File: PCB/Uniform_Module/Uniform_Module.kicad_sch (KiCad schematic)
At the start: 159 parts, among them U1 STM32L072KZT6, U2 SN74AHCT1G125DBVR

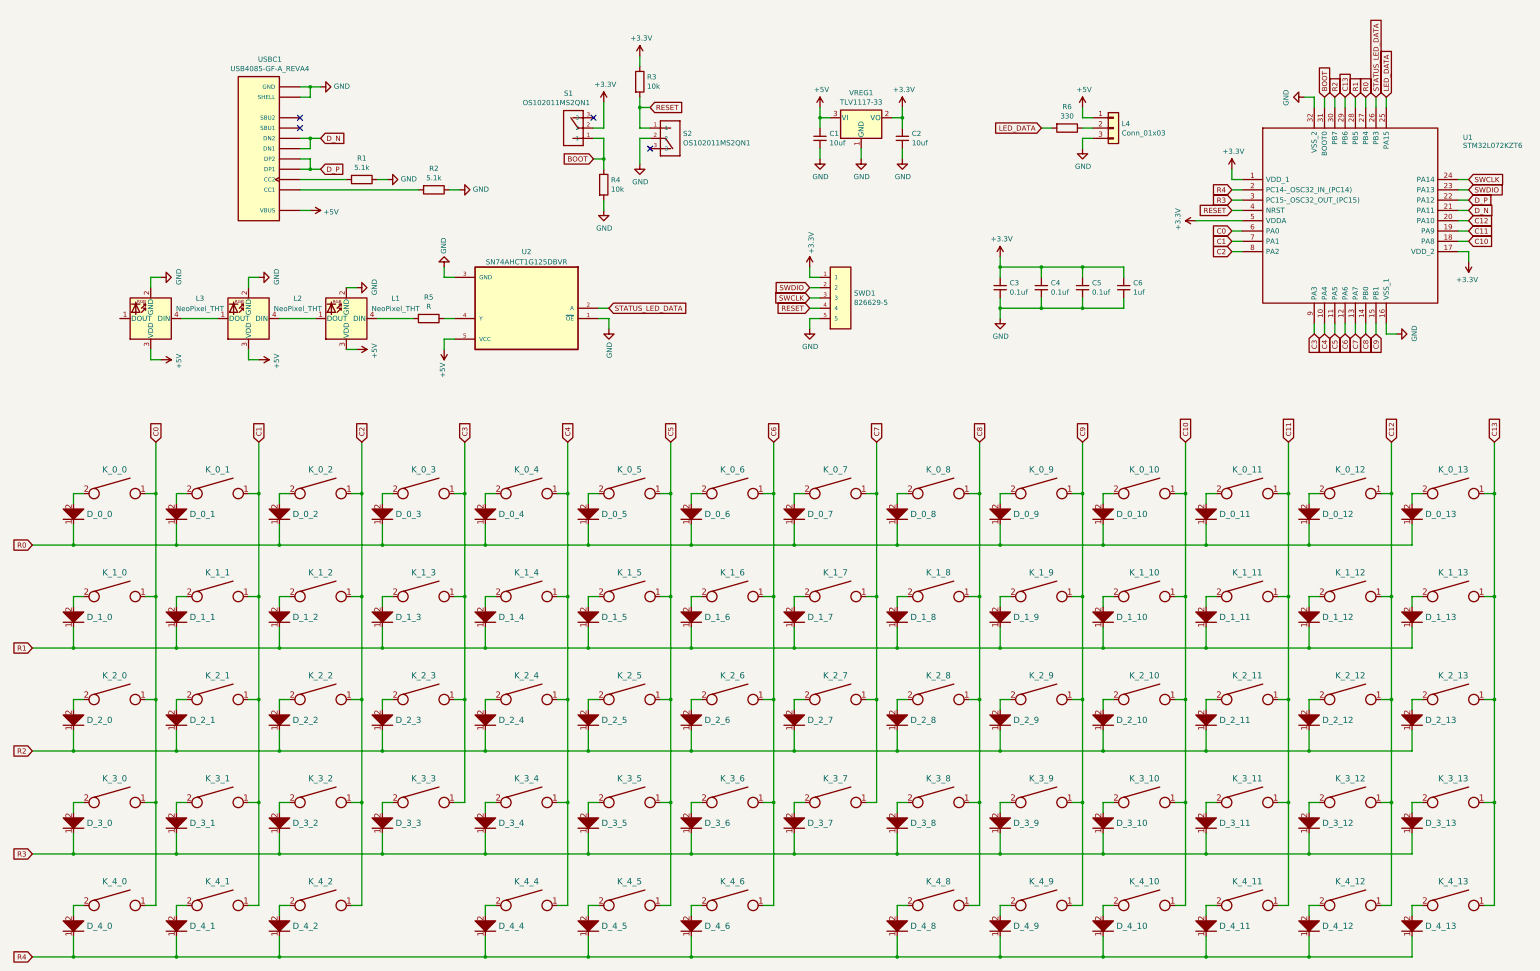
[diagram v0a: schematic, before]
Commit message: broke Uniform into two projects - uniform_board and uniform_module. Finished uniform_module schematic
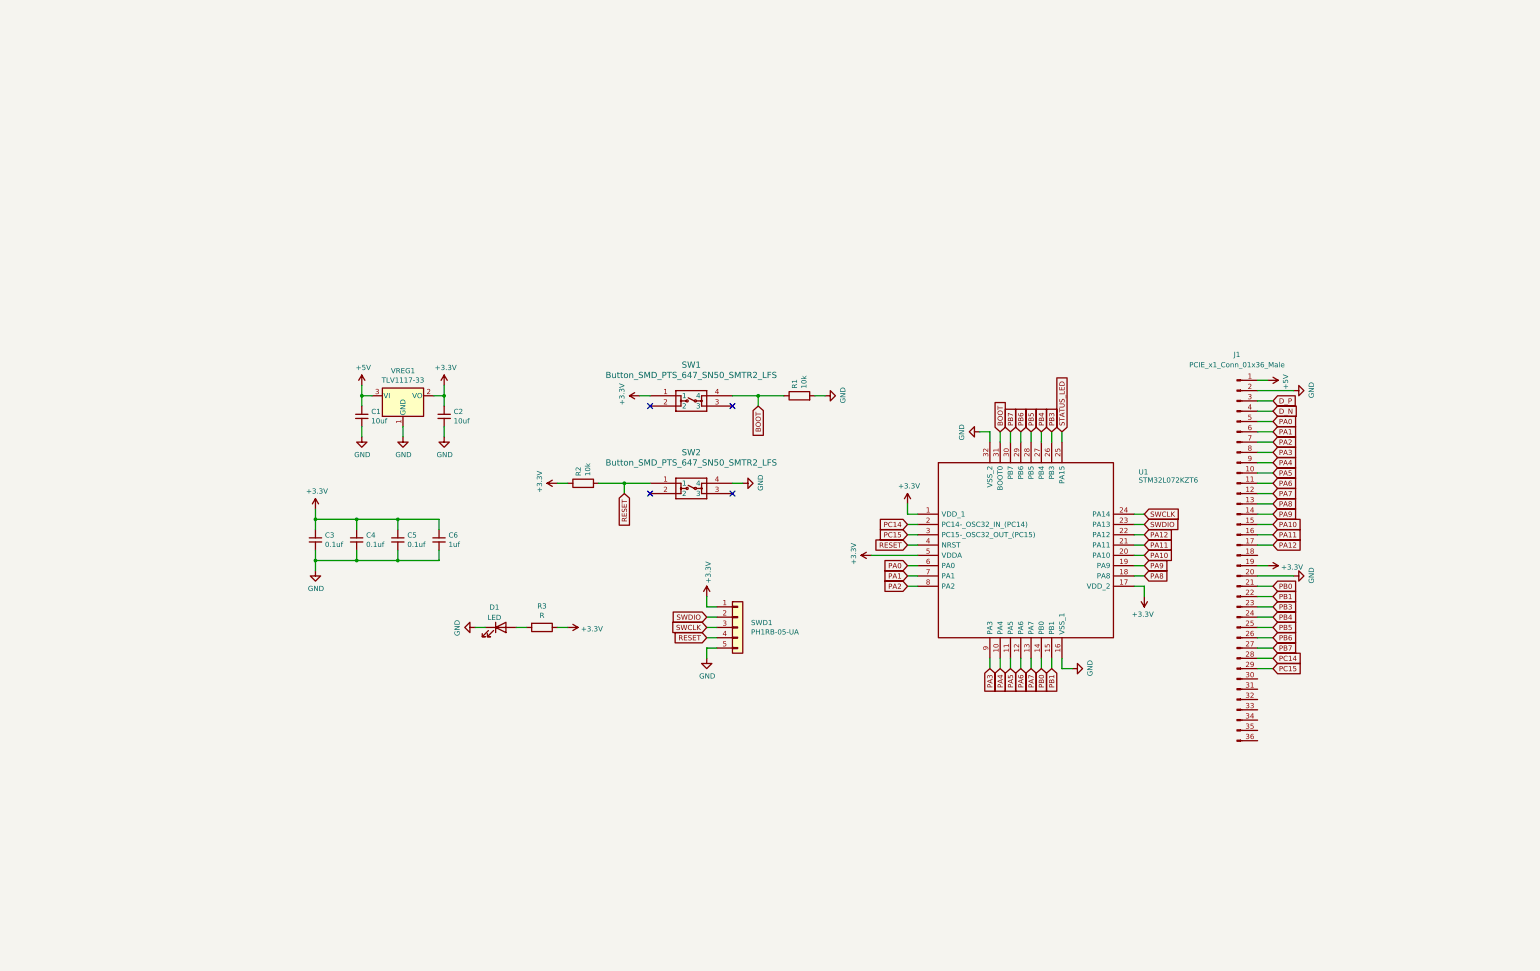
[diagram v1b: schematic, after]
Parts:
- removed D_0_0, D_0_1, D_0_10, D_0_11, D_0_12, D_0_13, D_0_2, D_0_3, D_0_4, D_0_5, D_0_6, D_0_7, D_0_8, D_0_9, D_1_0, D_1_1, D_1_10, D_1_11, D_1_12, D_1_13, D_1_2, D_1_3, D_1_4, D_1_5, D_1_6, D_1_7, D_1_8, D_1_9, D_2_0, D_2_1, D_2_10, D_2_11, D_2_12, D_2_13, D_2_2, D_2_3, D_2_4, D_2_5, D_2_6, D_2_7, D_2_8, D_2_9, D_3_0, D_3_1, D_3_10, D_3_11, D_3_12, D_3_13, D_3_2, D_3_3, D_3_4, D_3_5, D_3_6, D_3_7, D_3_8, D_3_9, D_4_0, D_4_1, D_4_10, D_4_11, D_4_12, D_4_13, D_4_2, D_4_4, D_4_5, D_4_6, D_4_8, D_4_9: D, 1N4148:DIOAD829W49L456D191, symbol keyboard_parts:D
- removed K_0_0, K_0_1, K_0_10, K_0_11, K_0_12, K_0_13, K_0_2, K_0_3, K_0_4, K_0_5, K_0_6, K_0_7, K_0_8, K_0_9, K_1_0, K_1_1, K_1_10, K_1_11, K_1_12, K_1_13, K_1_2, K_1_3, K_1_4, K_1_5, K_1_6, K_1_7, K_1_8, K_1_9, K_2_0, K_2_1, K_2_10, K_2_11, K_2_12, K_2_13, K_2_2, K_2_3, K_2_4, K_2_5, K_2_6, K_2_7, K_2_8, K_2_9, K_3_0, K_3_1, K_3_10, K_3_11, K_3_12, K_3_13, K_3_2, K_3_3, K_3_4, K_3_5, K_3_6, K_3_7, K_3_8, K_3_9, K_4_0, K_4_1, K_4_10, K_4_11, K_4_12, K_4_13, K_4_2, K_4_4, K_4_5, K_4_6, K_4_8, K_4_9: KEYSW, keyswitches:SW_MX, symbol keyboard_parts:KEYSW
- removed L1, L2, L3: NeoPixel_THT, Neopixel:LED_D5.0mm-4_RGB, symbol LED:NeoPixel_THT
- removed L4: Conn_01x03, Connector_PinHeader_2.54mm:PinHeader_1x03_P2.54mm_Vertical, symbol Connector_Generic:Conn_01x03
- removed R3, R4: 10k, Resistor_THT:R_Axial_DIN0204_L3.6mm_D1.6mm_P7.62mm_Horizontal, symbol Device:R
- removed R6: 330, Resistor_THT:R_Axial_DIN0309_L9.0mm_D3.2mm_P12.70mm_Horizontal, symbol Device:R
- removed S1, S2: OS102011MS2QN1, OS102011MS2QN1:SW_OS102011MS2QN1, symbol OS102011MS2QN1:OS102011MS2QN1
- removed U2: SN74AHCT1G125DBVR, SN74AHCT1G125DBVR:SOT95P280X145-5N, symbol SN74AHCT1G125DBVR:SN74AHCT1G125DBVR
- removed USBC1: USB4085-GF-A_REVA4, USB4085-GF-A_REVA4:GCT_USB4085-GF-A_REVA4, symbol USB4085-GF-A_REVA4:USB4085-GF-A_REVA4
- added D1: LED, symbol Device:LED
- added J1: PCIE_x1_Conn_01x36_Male, symbol Connector:Conn_01x36_Male
- added SW1, SW2: Button_SMD_PTS_647_SN50_SMTR2_LFS, PTS 647 SN50 SMTR2 LFS, symbol Uniform:Button_SMD_PTS_647_SN50_SMTR2_LFS
- R1, R2: value 5.1k -> 10k
- SWD1: value 826629-5 -> PH1RB-05-UA; symbol 826629-5:826629-5 -> Connector_Generic:Conn_01x05
- renumbered R5 to R3
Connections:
- net +3V3: now also R2.1, R3.1, J1.19 (Pin_19), SW1.1
- net +5V: now also J1.1 (Pin_1)
- net BOOT: now also R1.1, SW1.4
- net D_N: now also J1.4 (Pin_4); no longer U1.21 (PA11)
- net D_P: now also J1.3 (Pin_3); no longer U1.22 (PA12)
- net GND: now also R1.2, D1.1 (K), J1.2 (Pin_2), J1.20 (Pin_20), SW2.4; no longer R1.1, R2.1
- net RESET: now also R2.2, SW2.1
- net at R3.2: now also D1.2 (A)
- net C0 renamed PA0
- net PA0: now also J1.5 (Pin_5)
- net C1 renamed PA1
- net PA1: now also J1.6 (Pin_6)
- net C10 renamed PA8
- net PA8: now also J1.13 (Pin_13)
- net C11 renamed PA9
- net PA9: now also J1.14 (Pin_14)
- net C12 renamed PA10
- net PA10: now also J1.15 (Pin_15)
- net C13 renamed PB6
- net PB6: now also J1.26 (Pin_26)
- net C2 renamed PA2
- net PA2: now also J1.7 (Pin_7)
- net C3 renamed PA3
- net PA3: now also J1.8 (Pin_8)
- net C4 renamed PA4
- net PA4: now also J1.9 (Pin_9)
- net C5 renamed PA5
- net PA5: now also J1.10 (Pin_10)
- net C6 renamed PA6
- net PA6: now also J1.11 (Pin_11)
- net C7 renamed PA7
- net PA7: now also J1.12 (Pin_12)
- net C8 renamed PB0
- net PB0: now also J1.21 (Pin_21)
- net C9 renamed PB1
- net PB1: now also J1.22 (Pin_22)
- net LED_DATA renamed STATUS_LED
- net R0 renamed PB4
- net PB4: now also J1.24 (Pin_24)
- net R1 renamed PB5
- net PB5: now also J1.25 (Pin_25)
- net R2 renamed PB7
- net PB7: now also J1.27 (Pin_27)
- net R3 renamed PC15
- net PC15: now also J1.29 (Pin_29)
- net R4 renamed PC14
- net PC14: now also J1.28 (Pin_28)
- net STATUS_LED_DATA renamed PB3
- net PB3: now also J1.23 (Pin_23)
- new net PA11: J1.16 (Pin_16), U1.21 (PA11)
- new net PA12: J1.17 (Pin_17), U1.22 (PA12)
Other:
- moved on the sheet: C1, C2, C3, C4, C5, C6, R3, SWD1, U1, VREG1

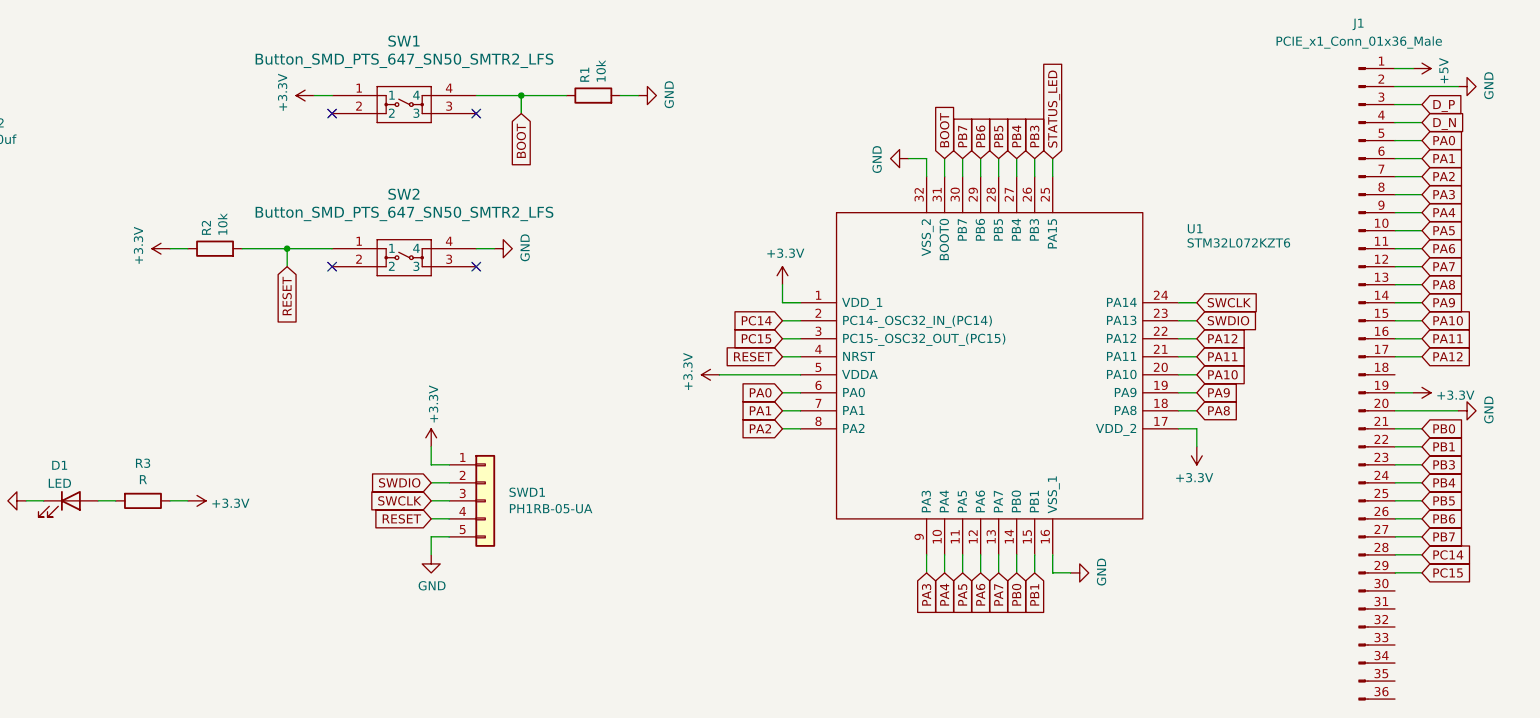
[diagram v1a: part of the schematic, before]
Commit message: PCIE slot is upside down... began footprint, comitting changes and preparing to re-route on board :(
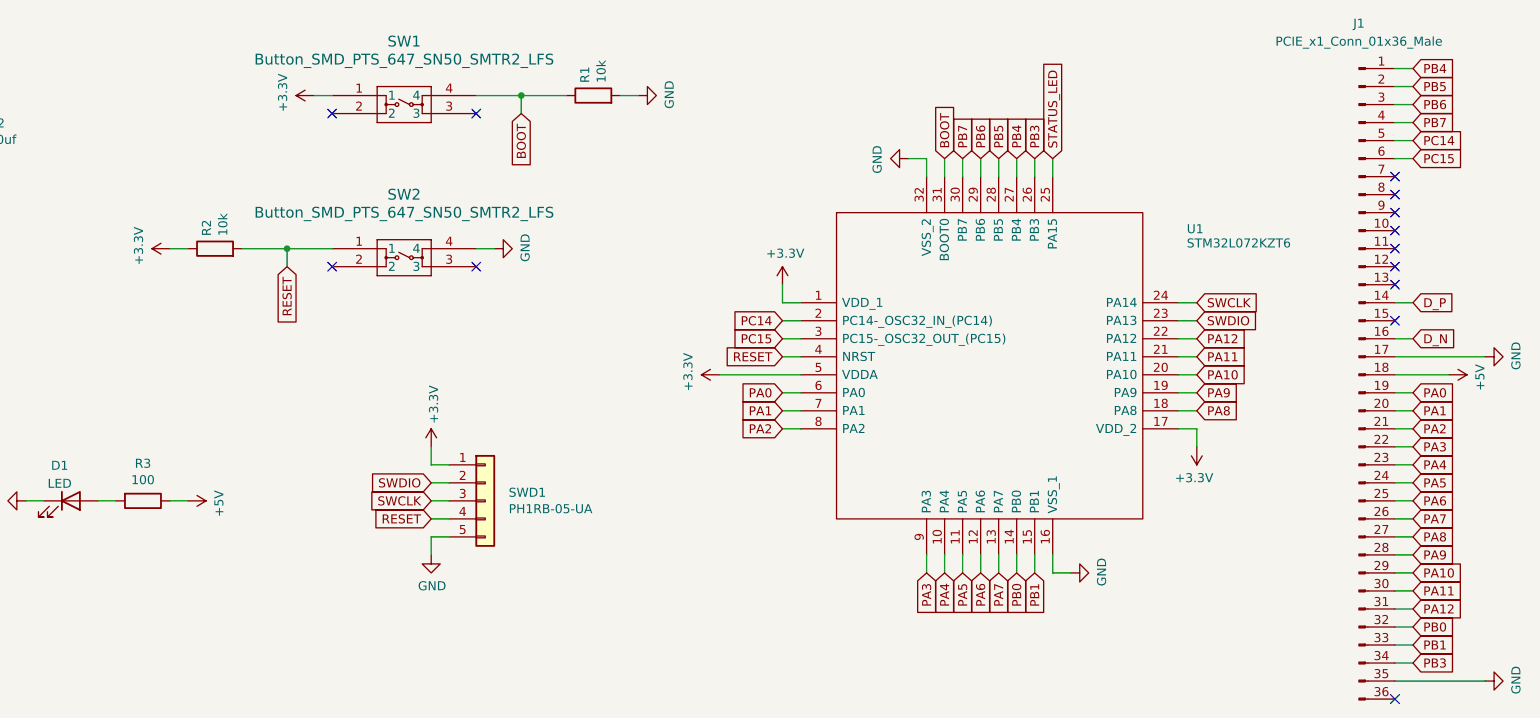
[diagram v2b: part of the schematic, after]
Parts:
- C1, C2: footprint ul_FG16X7R1E106KRT06:FG16X7R1E106KRT06 -> Capacitor_SMD:C_0603_1608Metric_Pad1.08x0.95mm_HandSolder
- C3, C4, C5: footprint Resistor_THT:R_Axial_DIN0207_L6.3mm_D2.5mm_P7.62mm_Horizontal -> Capacitor_SMD:C_0603_1608Metric_Pad1.08x0.95mm_HandSolder
- C6: footprint RDER71H105K2M1H03A:CAP_RDER71H105K2M1H03A -> Capacitor_SMD:C_0603_1608Metric_Pad1.08x0.95mm_HandSolder
- D1: footprint (none) -> LED_SMD:LED_0603_1608Metric_Pad1.05x0.95mm_HandSolder
- R1, R2: footprint Resistor_THT:R_Axial_DIN0204_L3.6mm_D1.6mm_P7.62mm_Horizontal -> Resistor_SMD:R_0603_1608Metric_Pad0.98x0.95mm_HandSolder
- R3: value R -> 100; footprint Resistor_THT:R_Axial_DIN0309_L9.0mm_D3.2mm_P12.70mm_Horizontal -> Resistor_SMD:R_0603_1608Metric_Pad0.98x0.95mm_HandSolder
- SWD1: footprint 826629-5:TE_826629-5 -> Connector_PinHeader_2.54mm:PinHeader_1x05_P2.54mm_Vertical
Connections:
- net +3V3: no longer J1.19 (Pin_19), R3.1
- net +5V: now also J1.18 (Pin_18), R3.1; no longer J1.1 (Pin_1)
- net D_N: now also J1.16 (Pin_16); no longer J1.4 (Pin_4)
- net D_P: now also J1.14 (Pin_14); no longer J1.3 (Pin_3)
- net GND: now also J1.17 (Pin_17), J1.35 (Pin_35); no longer J1.2 (Pin_2), J1.20 (Pin_20)
- net PA0: now also J1.19 (Pin_19); no longer J1.5 (Pin_5)
- net PA1: now also J1.20 (Pin_20); no longer J1.6 (Pin_6)
- net PA10: now also J1.29 (Pin_29); no longer J1.15 (Pin_15)
- net PA11: now also J1.30 (Pin_30); no longer J1.16 (Pin_16)
- net PA12: now also J1.31 (Pin_31); no longer J1.17 (Pin_17)
- net PA2: now also J1.21 (Pin_21); no longer J1.7 (Pin_7)
- net PA3: now also J1.22 (Pin_22); no longer J1.8 (Pin_8)
- net PA4: now also J1.23 (Pin_23); no longer J1.9 (Pin_9)
- net PA5: now also J1.24 (Pin_24); no longer J1.10 (Pin_10)
- net PA6: now also J1.25 (Pin_25); no longer J1.11 (Pin_11)
- net PA7: now also J1.26 (Pin_26); no longer J1.12 (Pin_12)
- net PA8: now also J1.27 (Pin_27); no longer J1.13 (Pin_13)
- net PA9: now also J1.28 (Pin_28); no longer J1.14 (Pin_14)
- net PB0: now also J1.32 (Pin_32); no longer J1.21 (Pin_21)
- net PB1: now also J1.33 (Pin_33); no longer J1.22 (Pin_22)
- net PB3: now also J1.34 (Pin_34); no longer J1.23 (Pin_23)
- net PB4: now also J1.1 (Pin_1); no longer J1.24 (Pin_24)
- net PB5: now also J1.2 (Pin_2); no longer J1.25 (Pin_25)
- net PB6: now also J1.3 (Pin_3); no longer J1.26 (Pin_26)
- net PB7: now also J1.4 (Pin_4); no longer J1.27 (Pin_27)
- net PC14: now also J1.5 (Pin_5); no longer J1.28 (Pin_28)
- net PC15: now also J1.6 (Pin_6); no longer J1.29 (Pin_29)
- no-connect marks 4 -> 13
